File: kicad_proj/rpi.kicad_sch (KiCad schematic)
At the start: 17 parts, among them J10 Conn_01x06, J11 Conn_01x04, J4 Raspberry_Pi_4, J5 Conn_01x02, J6 Conn_01x04, J7 Conn_01x04, J8 Conn_01x04, J9 Conn_01x06, U3 CAT24C32WI-GT3

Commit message: checked root, dc dc and rpi sheets
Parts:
- removed J10, J9: Conn_01x06, Connector_PinHeader_1.00mm:PinHeader_1x06_P1.00mm_Vertical, symbol Connector_Generic:Conn_01x06
- removed J11, J8: Conn_01x04, Connector_PinHeader_1.00mm:PinHeader_1x04_P1.00mm_Vertical, symbol Connector_Generic:Conn_01x04
- removed J4: Raspberry_Pi_4, rpi_power_warden_hat:RPI_Hat_B+, symbol Connector:Raspberry_Pi_4
- added J4: Raspberry Pi SMT connector, rpi_power_warden_hat:rpi_hat_smt, symbol rpi_power_warden_hat:rpi_hat_smt
- J5: now not fitted; now left out of the parts list
- renumbered TP12 to TP6, TP11 to TP7
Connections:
- net +3V3: now also J4.1 (3V3), J4.17 (3V3)
- net +5V_RPI: now also J4.2 (5V), J4.4 (5V)
- net CE0_SPI0/GPIO08: now also J4.24 (~{CE0}_SPI0/GPIO08)
- net ENA_5V_SW: now also J4.29 (GPCLK1/GPIO05)
- net ENA_VBAT_SW: now also J4.26 (~{CE1}_SPI0/GPIO07)
- net GND: now also J4.14 (GND), J4.20 (GND), J4.25 (GND), J4.30 (GND), J4.34 (GND), J4.39 (GND), J4.6 (GND), J4.9 (GND)
- net GPCLK2/GPIO06: now also J4.31 (GPCLK2/GPIO06)
- net GPIO12/PWM0: now also J4.32 (GPIO12/PWM0)
- net GPIO13/PWM1: now also J4.33 (GPIO13/PWM1)
- net GPIO14/UART_TXD: now also J4.8 (GPIO14/UART_TXD)
- net GPIO15/UART_RXD: now also J4.10 (GPIO15/UART_RXD)
- net GPIO16/SP1_CE2: now also J4.36 (GPIO16/SPI1_~{CE2})
- net GPIO18/SPI1_CE0: now also J4.12 (GPIO18/SPI1_~{CE0}/PCM_CLK/PWM0)
- net GPIO19/SPI1_MISO: now also J4.35 (GPIO19/SPI1_MISO/PCM_FS)
- net GPIO20/SPI1_MOSI: now also J4.38 (GPIO20/SPI1_MOSI/PCM_DIN/PWM1)
- net GPIO21/SPI1_CLK: now also J4.40 (GPIO21/SPI1_SCLK/PCM_DOUT)
- net GPIO22/SDIO_CLK: now also J4.15 (GPIO22/SDIO_CLK)
- net GPIO23/SDIO_CMD: now also J4.16 (GPIO23/SDIO_CMD)
- net GPIO24/SDIO_DAT0: now also J4.18 (GPIO24/SDIO_DAT0)
- net GPIO25/SDIO_DAT1: now also J4.22 (GPIO25/SDIO_DAT1)
- net GPIO26/SDIO_DAT2: now also J4.37 (GPIO26/SDIO_DAT2)
- net GPIO27/SDIO_DAT3: now also J4.13 (GPIO27/SDIO_DAT3)
- net ID_SC_I2C0: now also J4.28 (ID_SC_I2C0/GPIO01)
- net ID_SD_I2C0: now also J4.27 (ID_SD_I2C0/GPIO00)
- net INA_5V_ALERT: now also J4.7 (GPCLK0/GPIO04)
- net INA_SCL: now also J4.5 (SCL_I2C1/GPIO03)
- net INA_SDA: now also J4.3 (SDA_I2C1/GPIO02)
- net INA_VBAT_ALERT: now also J4.11 (GPIO17/SPI1_~{CE1})
- net MISO_SPI0/GPIO09: now also J4.21 (MISO_SPI0/GPIO09)
- net MOSI_SPI0/GPIO10: now also J4.19 (MOSI_SPI0/GPIO10)
- net SCLK_SPI0/GPIO11: now also J4.23 (SCLK_SPI0/GPIO11)
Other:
- note removed: "Extra GPIO headers"
- moved on the sheet: J6, J7

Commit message: checked all the schematics
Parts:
- TP6, TP7: now left out of the parts list
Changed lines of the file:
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@@
 		(unit 1)
 		(exclude_from_sim no)
-		(in_bom yes)
+		(in_bom no)
 		(on_board yes)
 		(dnp no)
@@
 		(unit 1)
 		(exclude_from_sim no)
-		(in_bom yes)
+		(in_bom no)
 		(on_board yes)
 		(dnp no)

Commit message: remove whitespaces from some resistors's mpn, add mpn to pnp in zvd symbol and regenerate bom
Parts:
- R5, R6: mpn ERJ-3EKF3901V -> ERJ-3EKF3901V
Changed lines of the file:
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@@
 			)
 		)
-		(property "mpn" " ERJ-3EKF3901V"
+		(property "mpn" "ERJ-3EKF3901V"
 			(at 199.39 59.69 0)
 			(effects
@@
 			)
 		)
-		(property "mpn" " ERJ-3EKF3901V"
+		(property "mpn" "ERJ-3EKF3901V"
 			(at 189.23 59.69 0)
 			(effects

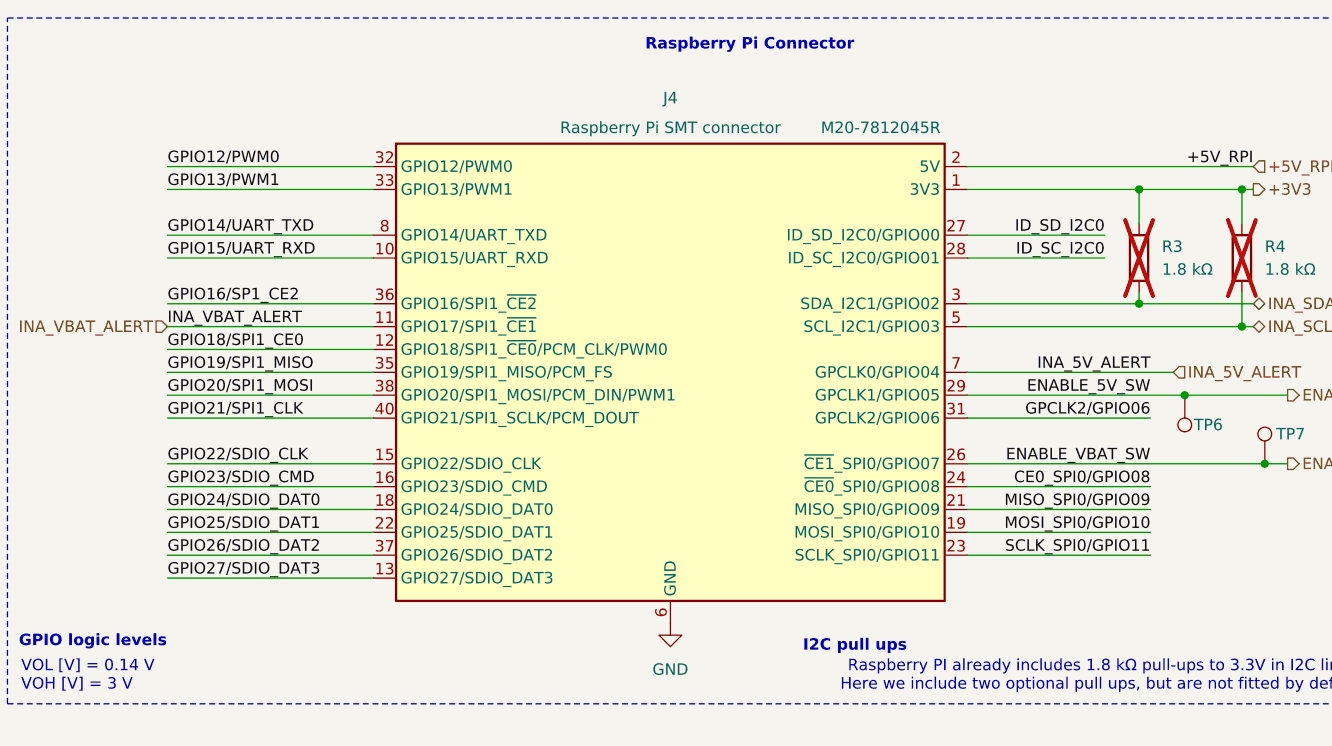
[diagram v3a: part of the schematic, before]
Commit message: run ERC and fix some errors (no critical errors, mostly associated to raspberry pi connectors not connected and with not NC flag
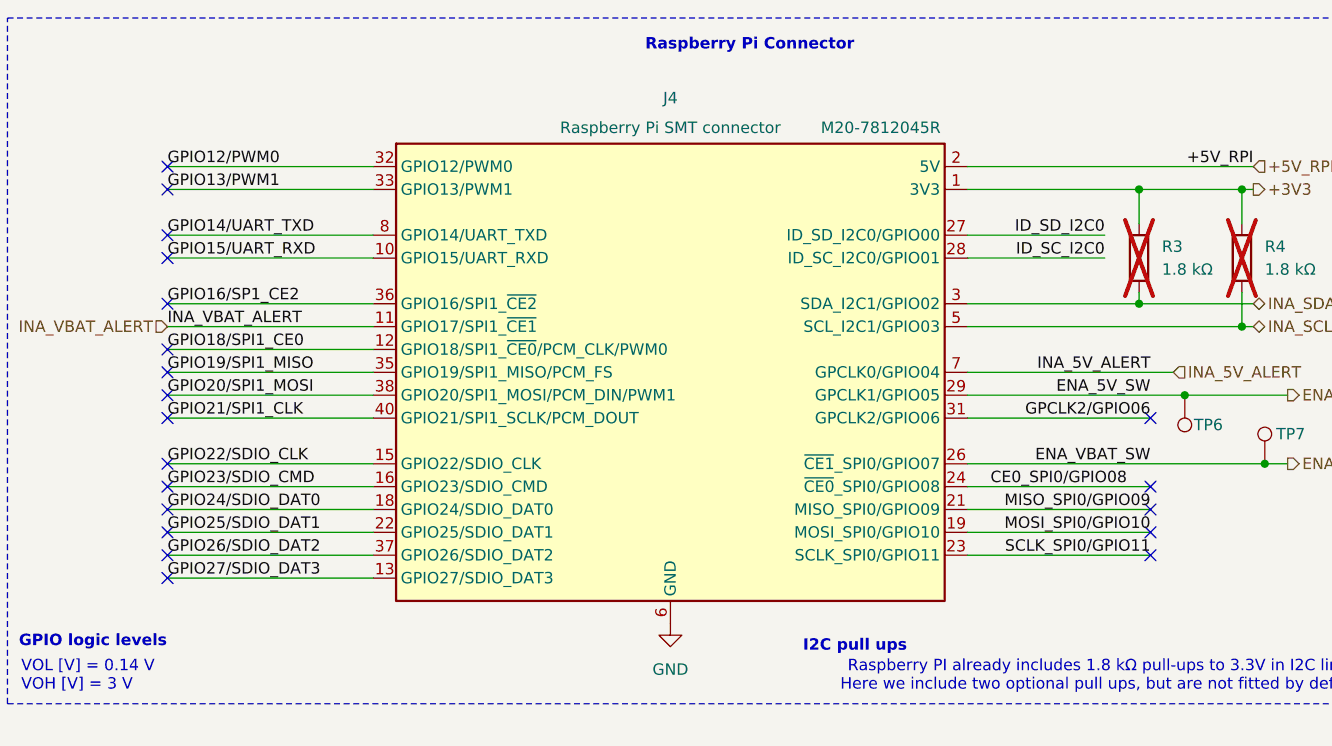
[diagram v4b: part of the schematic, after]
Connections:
- no-connect marks 0 -> 20
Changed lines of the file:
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@@
 		(color 0 0 0 0)
 	)
+	(no_connect
+		(at 33.02 80.01)
+	)
+	(no_connect
+		(at 33.02 100.33)
+	)
+	(no_connect
+		(at 142.24 92.71)
+	)
+	(no_connect
+		(at 33.02 87.63)
+	)
+	(no_connect
+		(at 33.02 92.71)
+	)
+	(no_connect
+		(at 33.02 82.55)
+	)
+	(no_connect
+		(at 142.24 97.79)
+	)
+	(no_connect
+		(at 33.02 77.47)
+	)
+	(no_connect
+		(at 33.02 74.93)
+	)
+	(no_connect
+		(at 33.02 62.23)
+	)
+	(no_connect
+		(at 142.24 90.17)
+	)
+	(no_connect
+		(at 33.02 69.85)
+	)
+	(no_connect
+		(at 33.02 97.79)
+	)
+	(no_connect
+		(at 142.24 95.25)
+	)
+	(no_connect
+		(at 142.24 82.55)
+	)
+	(no_connect
+		(at 33.02 90.17)
+	)
+	(no_connect
+		(at 33.02 64.77)
+	)
+	(no_connect
+		(at 33.02 95.25)
+	)
+	(no_connect
+		(at 33.02 54.61)
+	)
+	(no_connect
+		(at 33.02 57.15)
+	)
 	(wire
 		(pts
@@
 		)
 	)
-	(label "ENABLE_VBAT_SW"
+	(label "ENA_VBAT_SW"
 		(at 142.24 87.63 180)
 		(effects
@@
 		)
 	)
-	(label "CE0_SPI0{slash}GPIO08"
-		(at 142.24 90.17 180)
+	(label "GPIO27{slash}SDIO_DAT3"
+		(at 33.02 100.33 0)
 		(effects
 			(font
 				(size 1.27 1.27)
 			)
-			(justify right bottom)
+			(justify left bottom)
 		)
 	)
-	(label "GPIO27{slash}SDIO_DAT3"
-		(at 33.02 100.33 0)
+	(label "CE0_SPI0{slash}GPIO08"
+		(at 124.46 90.17 0)
 		(effects
 			(font
@@
 		)
 	)
-	(label "ENABLE_5V_SW"
+	(label "ENA_5V_SW"
 		(at 142.24 80.01 180)
 		(effects

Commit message: add footprint to j5
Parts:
- J5: footprint (none) -> Connector_PinHeader_2.54mm:PinHeader_1x02_P2.54mm_Vertical
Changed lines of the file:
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@@
 			)
 		)
-		(property "Footprint" ""
+		(property "Footprint" "Connector_PinHeader_2.54mm:PinHeader_1x02_P2.54mm_Vertical"
 			(at 241.3 63.5 0)
 			(effects

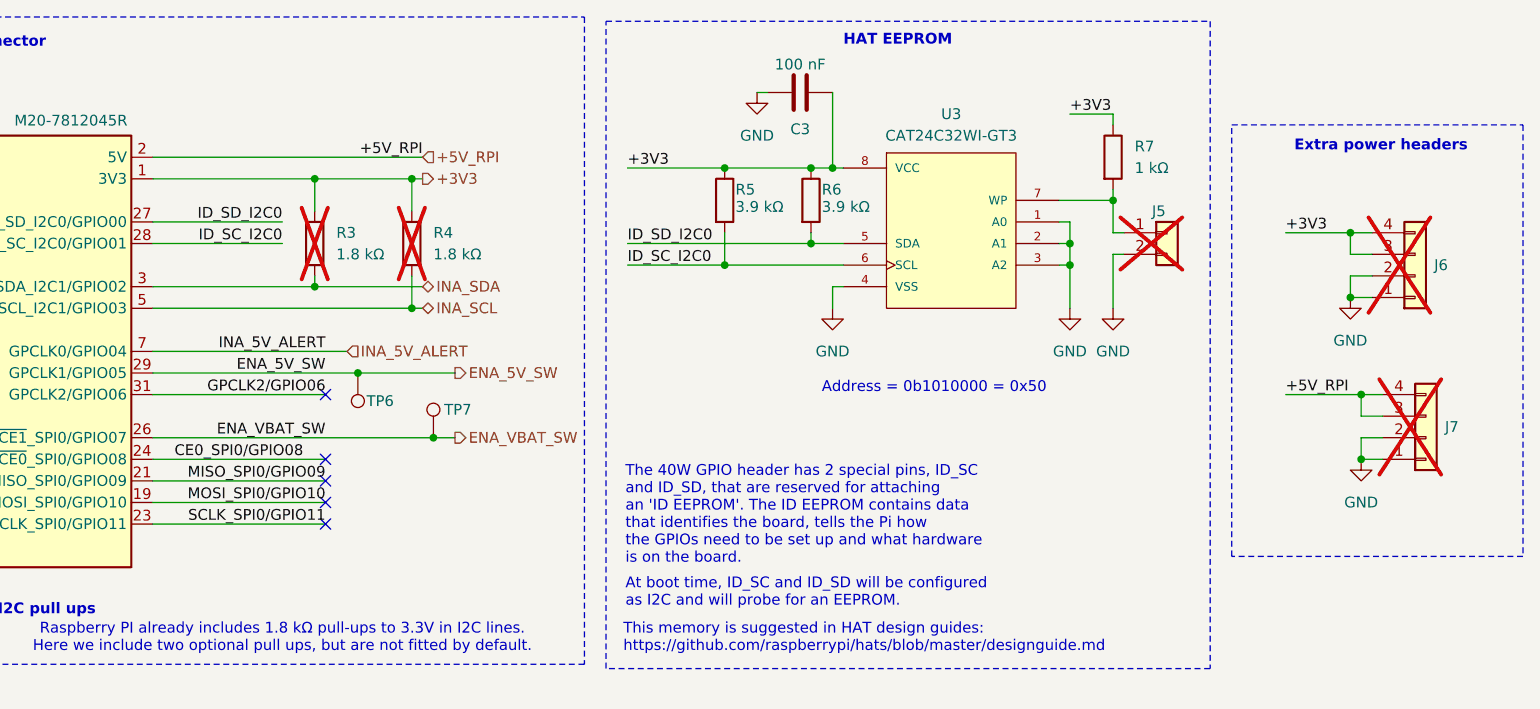
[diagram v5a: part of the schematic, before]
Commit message: finish placement
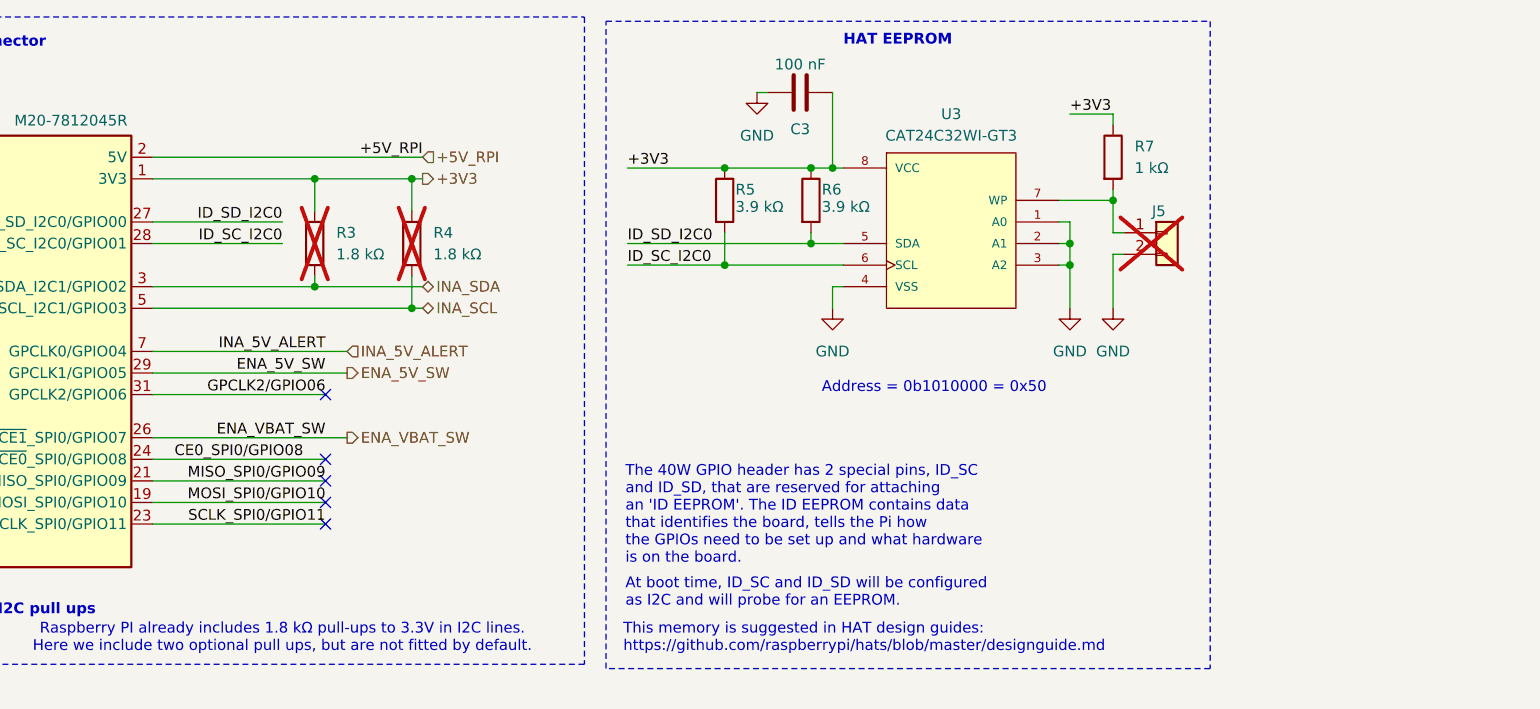
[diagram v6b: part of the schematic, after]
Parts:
- removed J6, J7: Conn_01x04, Connector_PinHeader_1.00mm:PinHeader_1x04_P1.00mm_Vertical, symbol Connector_Generic:Conn_01x04
- removed TP6, TP7: TestPoint, TestPoint:TestPoint_Pad_D2.5mm, symbol Connector:TestPoint
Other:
- note removed: "Extra power headers"
